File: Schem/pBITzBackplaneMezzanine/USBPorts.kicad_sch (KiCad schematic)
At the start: 30 parts, among them J1 USB3_A_Stacked, J2 Conn_01x04, J3 Conn_01x04, U1 FE1.1S-BSOP28BCN, U2 MAX3421EETJ_T, U3 CD74HC4050M96, Y1 ABL-12.000MHZ-B2, Y2 ABL-12.000MHZ-B2

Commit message: synching
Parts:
- J2, J3: footprint Connector_PinSocket_2.54mm:PinSocket_1x04_P2.54mm_Vertical -> Connector_PinHeader_2.54mm:PinHeader_1x04_P2.54mm_Vertical
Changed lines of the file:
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@@
 			)
 		)
-		(property "Footprint" "Connector_PinSocket_2.54mm:PinSocket_1x04_P2.54mm_Vertical"
+		(property "Footprint" "Connector_PinHeader_2.54mm:PinHeader_1x04_P2.54mm_Vertical"
 			(at 275.59 125.73 0)
 			(effects
@@
 			)
 		)
-		(property "Footprint" "Connector_PinSocket_2.54mm:PinSocket_1x04_P2.54mm_Vertical"
+		(property "Footprint" "Connector_PinHeader_2.54mm:PinHeader_1x04_P2.54mm_Vertical"
 			(at 344.17 125.73 0)
 			(effects

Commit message: Added all the manufacturer part numbers to the KiCad schematics and PCB files. This will make it easier to order the parts for the project and ensure that the correct components are used. I also removed some of the old schematics that were no longer needed, such as the BaudClock, ConsolePort, DeviceSelectDecode, GPIOUserSerial, IO Controller, UserPorts, Video, and Z80HomeBrew schematics. These changes will help to streamline the design and make it easier to understand.
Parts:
- J1: MANUFACTURER_PART_NUMBER (none) -> 0484060001
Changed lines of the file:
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@@
 			)
 		)
+		(property "MANUFACTURER_PART_NUMBER" "0484060001"
+			(at 387.35 52.07 0)
+			(effects
+				(font
+					(size 1.27 1.27)
+				)
+				(hide yes)
+			)
+		)
 		(pin "5"
 		)
@@
 			)
 		)
-		(property "Datasheet" "~"
+		(property "Datasheet" "C0603C104K5RACTU"
 			(at 147.32 34.29 0)
 			(effects
@@
 			)
 		)
+		(property "MANUFACTURER_PART_NUMBER" "0484060001"
+			(at 387.35 99.06 0)
+			(effects
+				(font
+					(size 1.27 1.27)
+				)
+				(hide yes)
+			)
+		)
 		(pin "5"
 		)
@@
 			)
 		)
-		(property "Datasheet" "~"
+		(property "Datasheet" "C0603C104K5RACTU"
 			(at 135.89 34.29 0)
 			(effects

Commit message: Updated the 3d images and exported the image
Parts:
- U3: footprint Footprints:SOIC127P600X175-16N -> Package_SO:SOIC-16_3.9x9.9mm_P1.27mm
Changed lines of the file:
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@@
 			)
 		)
-		(property "Footprint" "Footprints:SOIC127P600X175-16N"
+		(property "Footprint" "Package_SO:SOIC-16_3.9x9.9mm_P1.27mm"
 			(at 124.46 151.13 0)
 			(effects
@@
 			)
 		)
-		(property "Footprint" "Footprints:SOIC127P600X175-16N"
+		(property "Footprint" "Package_SO:SOIC-16_3.9x9.9mm_P1.27mm"
 			(at 82.55 144.78 0)
 			(effects
@@
 			)
 		)
-		(property "Footprint" "Footprints:SOIC127P600X175-16N"
+		(property "Footprint" "Package_SO:SOIC-16_3.9x9.9mm_P1.27mm"
 			(at 143.51 146.05 0)
 			(effects
@@
 			)
 		)
-		(property "Footprint" "Footprints:SOIC127P600X175-16N"
+		(property "Footprint" "Package_SO:SOIC-16_3.9x9.9mm_P1.27mm"
 			(at 82.55 162.56 0)
 			(effects
@@
 			)
 		)
-		(property "Footprint" "Footprints:SOIC127P600X175-16N"
+		(property "Footprint" "Package_SO:SOIC-16_3.9x9.9mm_P1.27mm"
 			(at 124.46 135.89 0)
 			(effects
@@
 			)
 		)
-		(property "Footprint" "Footprints:SOIC127P600X175-16N"
+		(property "Footprint" "Package_SO:SOIC-16_3.9x9.9mm_P1.27mm"
 			(at 82.55 129.54 0)
 			(effects
@@
 			)
 		)
-		(property "Footprint" "Footprints:SOIC127P600X175-16N"
+		(property "Footprint" "Package_SO:SOIC-16_3.9x9.9mm_P1.27mm"
 			(at 124.46 165.1 0)
 			(effects

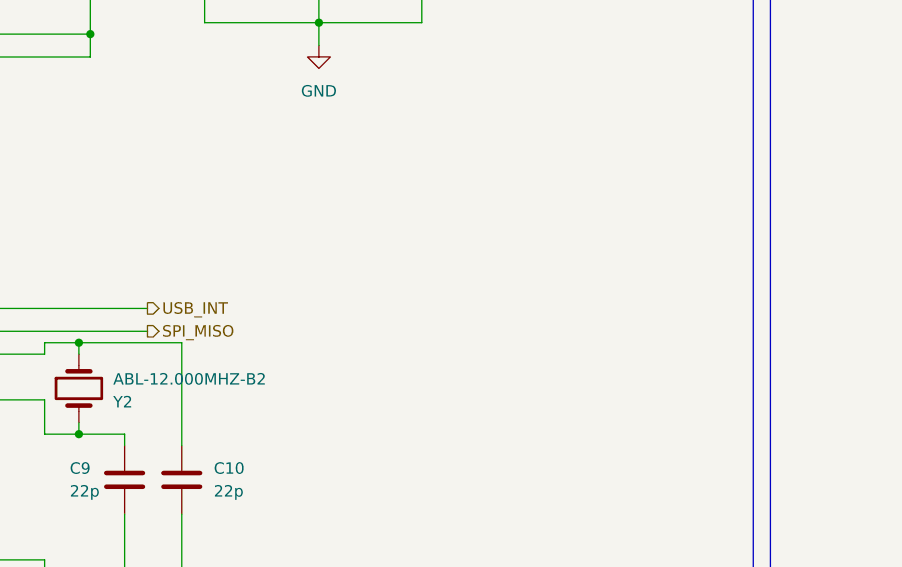
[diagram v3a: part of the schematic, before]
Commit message: Major rework:
- Updated the Mezzanine to remove the slot connector and move it to the main board (facing the back)
-    The removal of the slot allowed for the removal of the FPC connector, which was a
     major source of complexity. The mezzanine now only has the SD card and USB connectors,
     which are much cheaper and easier to work with.
- The mezzanine is now more compact and cheaper to souirce

- The main board sees the addition of the external slot connector (coming from the mezzanine)
- Added power led on the mother board for easier debugging and testing
- Removed the free floating resistors to replace them with resistor packs
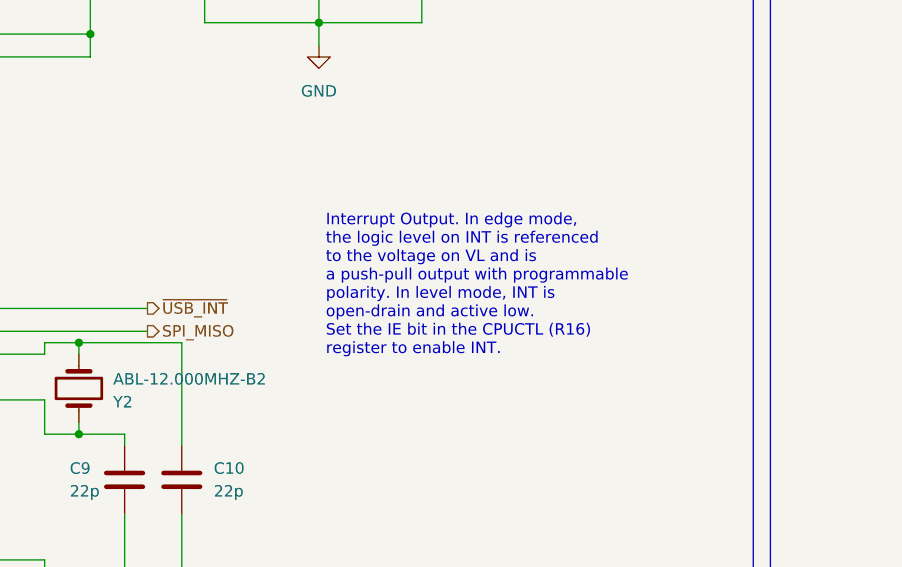
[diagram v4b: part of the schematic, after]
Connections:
- net USB_INT renamed ~{USB_INT}
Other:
- note added: "Interrupt Output. In edge mode, the logic level on INT is referenced to the voltage on VL and is a push-pull output with programmable polarity. In level mode, INT is open-drain and active low. Set the IE bit in the CPUCTL (R16) register to enable INT."
